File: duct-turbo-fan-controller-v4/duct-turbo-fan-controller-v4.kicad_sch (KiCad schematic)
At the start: 46 parts, among them J1 Screw_Terminal_01x04, J2 Conn_01x04, J3 USB_OTG, J4 AudioJack4, J7 Conn_01x04, Q1 MMBT3904, Q2 BSS84, SW1 SW_Push, SW2 SW_Push, U1 SCD41-D-R2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

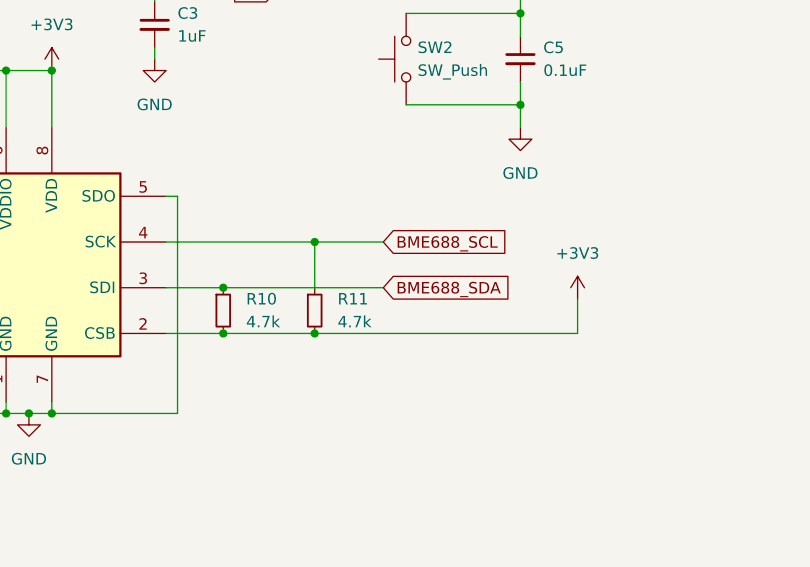
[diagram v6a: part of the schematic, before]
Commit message: Clean up to avoid overlapping wires.
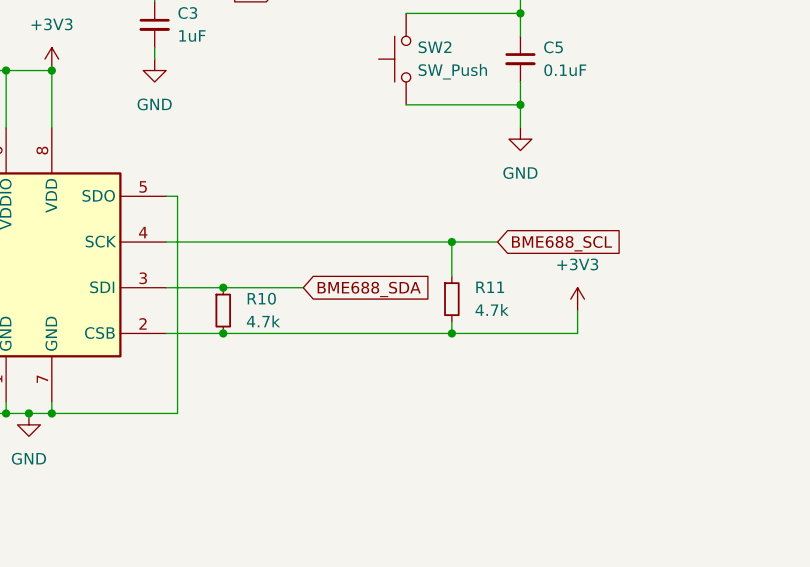
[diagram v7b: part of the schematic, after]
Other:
- moved on the sheet: R11
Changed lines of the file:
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@@
 	)
 	(junction
+		(at 196.85 59.69)
+		(diameter 0)
+		(color 0 0 0 0)
+	)
+	(junction
 		(at 243.84 102.87)
 		(diameter 0)
@@
 	)
 	(junction
+		(at 196.85 69.85)
+		(diameter 0)
+		(color 0 0 0 0)
+	)
+	(junction
 		(at 196.85 146.05)
 		(diameter 0)
@@
 	)
 	(junction
-		(at 181.61 59.69)
-		(diameter 0)
-		(color 0 0 0 0)
-	)
-	(junction
-		(at 181.61 69.85)
-		(diameter 0)
-		(color 0 0 0 0)
-	)
-	(junction
 		(at 64.77 36.83)
 		(diameter 0)
@@
 	(wire
 		(pts
+			(xy 196.85 69.85) (xy 210.82 69.85)
+		)
+		(stroke
+			(width 0)
+			(type default)
+		)
+	)
+	(wire
+		(pts
 			(xy 137.16 158.75) (xy 137.16 173.99)
 		)
@@
 	(wire
 		(pts
-			(xy 210.82 69.85) (xy 210.82 66.04)
+			(xy 210.82 69.85) (xy 210.82 67.31)
 		)
 		(stroke
@@
 	(wire
 		(pts
-			(xy 181.61 69.85) (xy 210.82 69.85)
-		)
-		(stroke
-			(width 0)
-			(type default)
-		)
-	)
-	(wire
-		(pts
 			(xy 254 161.29) (xy 237.49 161.29)
 		)
@@
 	(wire
 		(pts
+			(xy 171.45 64.77) (xy 180.34 64.77)
+		)
+		(stroke
+			(width 0)
+			(type default)
+		)
+	)
+	(wire
+		(pts
 			(xy 85.09 176.53) (xy 85.09 181.61)
 		)
@@
 	(wire
 		(pts
+			(xy 196.85 68.58) (xy 196.85 69.85)
+		)
+		(stroke
+			(width 0)
+			(type default)
+		)
+	)
+	(wire
+		(pts
 			(xy 156.21 189.23) (xy 146.05 189.23)
 		)
@@
 	(wire
 		(pts
-			(xy 181.61 64.77) (xy 181.61 59.69)
+			(xy 196.85 63.5) (xy 196.85 59.69)
 		)
 		(stroke
@@
 	(wire
 		(pts
-			(xy 171.45 69.85) (xy 181.61 69.85)
+			(xy 171.45 69.85) (xy 196.85 69.85)
 		)
 		(stroke
@@
 	(wire
 		(pts
-			(xy 181.61 59.69) (xy 189.23 59.69)
+			(xy 165.1 59.69) (xy 196.85 59.69)
 		)
 		(stroke
@@
 	(wire
 		(pts
-			(xy 181.61 59.69) (xy 165.1 59.69)
+			(xy 196.85 59.69) (xy 201.93 59.69)
 		)
 		(stroke
@@
 	(wire
 		(pts
-			(xy 171.45 64.77) (xy 189.23 64.77)
-		)
-		(stroke
-			(width 0)
-			(type default)
-		)
-	)
-	(wire
-		(pts
 			(xy 50.8 137.16) (xy 57.15 137.16)
 		)
@@
 	(global_label "BME688_SDA"
 		(shape input)
-		(at 189.23 64.77 0)
+		(at 180.34 64.77 0)
 		(fields_autoplaced yes)
 		(effects
@@
 		)
 		(property "Intersheetrefs" "${INTERSHEET_REFS}"
-			(at 204.2498 64.77 0)
+			(at 195.3598 64.77 0)
 			(effects
 				(font
@@
 	(global_label "BME688_SCL"
 		(shape input)
-		(at 189.23 59.69 0)
+		(at 201.93 59.69 0)
 		(fields_autoplaced yes)
 		(effects
@@
 		)
 		(property "Intersheetrefs" "${INTERSHEET_REFS}"
-			(at 204.1893 59.69 0)
+			(at 216.8893 59.69 0)
 			(effects
 				(font
@@
 	(symbol
 		(lib_id "Device:R_Small")
-		(at 181.61 67.31 0)
+		(at 196.85 66.04 0)
 		(unit 1)
 		(exclude_from_sim no)
@@
 		(fields_autoplaced yes)
 		(property "Reference" "R11"
-			(at 184.15 66.0399 0)
+			(at 199.39 64.7699 0)
 			(effects
 				(font
@@
 		)
 		(property "Value" "4.7k"
-			(at 184.15 68.5799 0)
+			(at 199.39 67.3099 0)
 			(effects
 				(font
@@
 		)
 		(property "Footprint" "Resistor_SMD:R_0603_1608Metric_Pad0.98x0.95mm_HandSolder"
-			(at 181.61 67.31 0)
+			(at 196.85 66.04 0)
 			(effects
 				(font
@@
 		)
 		(property "Datasheet" "~"
-			(at 181.61 67.31 0)
+			(at 196.85 66.04 0)
 			(effects
 				(font
@@
 		)
 		(property "Description" ""
-			(at 181.61 67.31 0)
+			(at 196.85 66.04 0)
 			(effects
 				(font
@@
 	(symbol
 		(lib_id "power:+3.3V")
-		(at 210.82 66.04 0)
+		(at 210.82 67.31 0)
 		(unit 1)
 		(exclude_from_sim no)
@@
 		(fields_autoplaced yes)
 		(property "Reference" "#PWR028"
-			(at 210.82 69.85 0)
+			(at 210.82 71.12 0)
 			(effects
 				(font
@@
 		)
 		(property "Value" "+3V3"
-			(at 210.82 60.96 0)
+			(at 210.82 62.23 0)
 			(effects
 				(font
@@
 		)
 		(property "Footprint" ""
-			(at 210.82 66.04 0)
+			(at 210.82 67.31 0)
 			(effects
 				(font
@@
 		)
 		(property "Datasheet" ""
-			(at 210.82 66.04 0)
+			(at 210.82 67.31 0)
 			(effects
 				(font
@@
 		)
 		(property "Description" ""
-			(at 210.82 66.04 0)
+			(at 210.82 67.31 0)
 			(effects
 				(font
